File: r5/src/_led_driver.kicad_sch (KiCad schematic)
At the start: 7 parts, among them J16 FH12A-20S-0.5SH, Q22 NX3008NBKW, U9 PCF8574PW

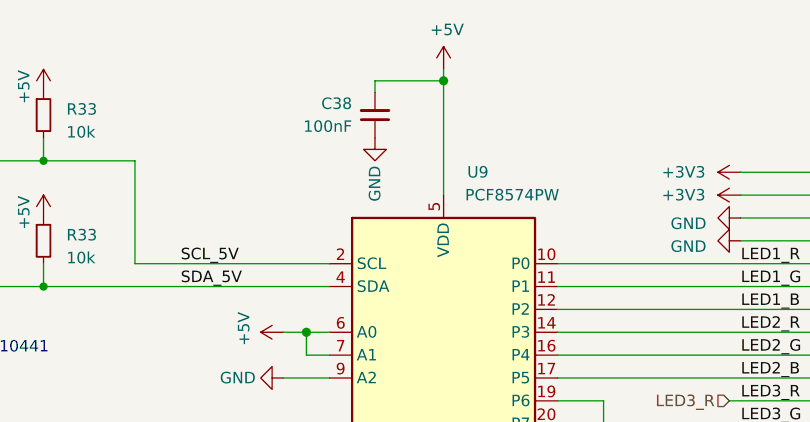
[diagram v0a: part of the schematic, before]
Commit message: Updates to +/-15V supply. Additional output capacitance. Change to smaller inductor packages. Add 0R links to permit isolation of output. Mods to compensation network. Set feedback resistors to datasheet values.
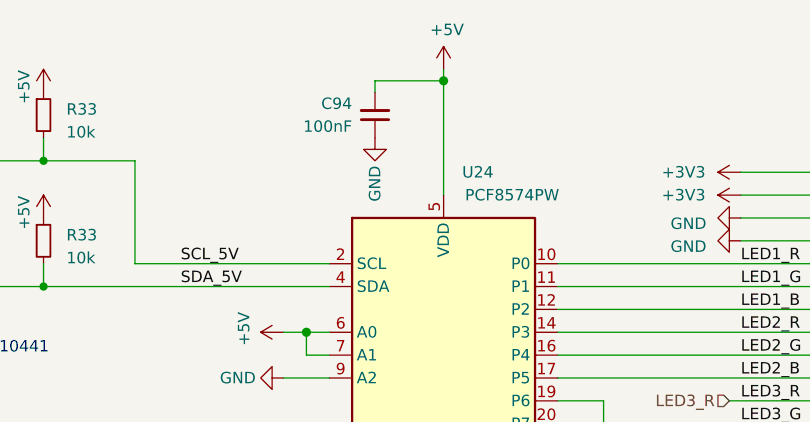
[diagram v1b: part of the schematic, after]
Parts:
- renumbered C38 to C94, U9 to U24
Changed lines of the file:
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@@
   (symbol (lib_id "Interface_Expansion:PCF8574TS") (at 142.24 69.85 0) (unit 1)
     (in_bom yes) (on_board yes) (dnp no)
-    (property "Reference" "U9" (at 146.05 49.53 0)
+    (property "Reference" "U24" (at 146.05 49.53 0)
       (effects (font (size 1.27 1.27)))
     )
@@
       (project "bugg-main-r5"
         (path "/e3eb514f-6ce4-4abe-ba20-f82f0015628f/676be2e4-179b-4538-a96d-4073cd6b4d31"
-          (reference "U9") (unit 1)
+          (reference "U24") (unit 1)
         )
       )
@@
         )
         (path "/e3eb514f-6ce4-4abe-ba20-f82f0015628f/676be2e4-179b-4538-a96d-4073cd6b4d31"
-          (reference "#PWR06") (unit 1)
+          (reference "#PWR0188") (unit 1)
         )
       )
@@
         )
         (path "/e3eb514f-6ce4-4abe-ba20-f82f0015628f/676be2e4-179b-4538-a96d-4073cd6b4d31"
-          (reference "#PWR02") (unit 1)
+          (reference "#PWR0193") (unit 1)
         )
       )
@@
   (symbol (lib_id "power:GND") (at 175.26 57.15 270) (unit 1)
     (in_bom yes) (on_board yes) (dnp no)
-    (property "Reference" "#PWR0125" (at 168.91 57.15 0)
+    (property "Reference" "#PWR0198" (at 168.91 57.15 0)
       (effects (font (size 1.27 1.27)) hide)
     )
@@
       (project "bugg-main-r5"
         (path "/e3eb514f-6ce4-4abe-ba20-f82f0015628f/676be2e4-179b-4538-a96d-4073cd6b4d31"
-          (reference "#PWR0125") (unit 1)
+          (reference "#PWR0198") (unit 1)
         )
       )
@@
   (symbol (lib_id "power:+3V3") (at 175.26 49.53 90) (unit 1)
     (in_bom yes) (on_board yes) (dnp no)
-    (property "Reference" "#PWR0127" (at 179.07 49.53 0)
+    (property "Reference" "#PWR0195" (at 179.07 49.53 0)
       (effects (font (size 1.27 1.27)) hide)
     )
@@
       (project "bugg-main-r5"
         (path "/e3eb514f-6ce4-4abe-ba20-f82f0015628f/676be2e4-179b-4538-a96d-4073cd6b4d31"
-          (reference "#PWR0127") (unit 1)
+          (reference "#PWR0195") (unit 1)
         )
       )
@@
         )
         (path "/e3eb514f-6ce4-4abe-ba20-f82f0015628f/676be2e4-179b-4538-a96d-4073cd6b4d31"
-          (reference "R79") (unit 1)
+          (reference "R66") (unit 1)
         )
       )
@@
   (symbol (lib_id "power:GND") (at 134.62 45.72 0) (unit 1)
     (in_bom yes) (on_board yes) (dnp no)
-    (property "Reference" "#PWR0120" (at 134.62 52.07 0)
+    (property "Reference" "#PWR0192" (at 134.62 52.07 0)
       (effects (font (size 1.27 1.27)) hide)
     )
@@
       (project "bugg-main-r5"
         (path "/e3eb514f-6ce4-4abe-ba20-f82f0015628f/676be2e4-179b-4538-a96d-4073cd6b4d31"
-          (reference "#PWR0120") (unit 1)
+          (reference "#PWR0192") (unit 1)
         )
       )
@@
         )
         (path "/e3eb514f-6ce4-4abe-ba20-f82f0015628f/676be2e4-179b-4538-a96d-4073cd6b4d31"
-          (reference "#PWR03") (unit 1)
+          (reference "#PWR0190") (unit 1)
         )
       )
@@
         )
         (path "/e3eb514f-6ce4-4abe-ba20-f82f0015628f/676be2e4-179b-4538-a96d-4073cd6b4d31"
-          (reference "Q28") (unit 1)
+          (reference "Q13") (unit 1)
         )
       )
@@
         )
         (path "/e3eb514f-6ce4-4abe-ba20-f82f0015628f/676be2e4-179b-4538-a96d-4073cd6b4d31"
-          (reference "R78") (unit 1)
+          (reference "R65") (unit 1)
         )
       )
@@
   (symbol (lib_id "power:+5V") (at 175.26 97.79 90) (unit 1)
     (in_bom yes) (on_board yes) (dnp no)
-    (property "Reference" "#PWR0124" (at 179.07 97.79 0)
+    (property "Reference" "#PWR0199" (at 179.07 97.79 0)
       (effects (font (size 1.27 1.27)) hide)
     )
@@
       (project "bugg-main-r5"
         (path "/e3eb514f-6ce4-4abe-ba20-f82f0015628f/676be2e4-179b-4538-a96d-4073cd6b4d31"
-          (reference "#PWR0124") (unit 1)
+          (reference "#PWR0199") (unit 1)
         )
       )
@@
         )
         (path "/e3eb514f-6ce4-4abe-ba20-f82f0015628f/676be2e4-179b-4538-a96d-4073cd6b4d31"
-          (reference "#PWR05") (unit 1)
+          (reference "#PWR0186") (unit 1)
         )
       )
@@
   (symbol (lib_id "Device:C_Small") (at 134.62 43.18 0) (mirror x) (unit 1)
     (in_bom yes) (on_board yes) (dnp no)
-    (property "Reference" "C38" (at 132.08 41.91 0)
+    (property "Reference" "C94" (at 132.08 41.91 0)
       (effects (font (size 1.27 1.27)) (justify right))
     )
@@
       (project "bugg-main-r5"
         (path "/e3eb514f-6ce4-4abe-ba20-f82f0015628f/676be2e4-179b-4538-a96d-4073cd6b4d31"
-          (reference "C38") (unit 1)
+          (reference "C94") (unit 1)
         )
       )
@@
   (symbol (lib_id "power:GND") (at 142.24 88.9 0) (unit 1)
     (in_bom yes) (on_board yes) (dnp no)
-    (property "Reference" "#PWR0117" (at 142.24 95.25 0)
+    (property "Reference" "#PWR0194" (at 142.24 95.25 0)
       (effects (font (size 1.27 1.27)) hide)
     )
@@
       (project "bugg-main-r5"
         (path "/e3eb514f-6ce4-4abe-ba20-f82f0015628f/676be2e4-179b-4538-a96d-4073cd6b4d31"
-          (reference "#PWR0117") (unit 1)
+          (reference "#PWR0194") (unit 1)
         )
       )
@@
         )
         (path "/e3eb514f-6ce4-4abe-ba20-f82f0015628f/676be2e4-179b-4538-a96d-4073cd6b4d31"
-          (reference "#PWR07") (unit 1)
+          (reference "#PWR0189") (unit 1)
         )
       )
@@
   (symbol (lib_id "power:+3V3") (at 175.26 52.07 90) (unit 1)
     (in_bom yes) (on_board yes) (dnp no)
-    (property "Reference" "#PWR0126" (at 179.07 52.07 0)
+    (property "Reference" "#PWR0196" (at 179.07 52.07 0)
       (effects (font (size 1.27 1.27)) hide)
     )
@@
       (project "bugg-main-r5"
         (path "/e3eb514f-6ce4-4abe-ba20-f82f0015628f/676be2e4-179b-4538-a96d-4073cd6b4d31"
-          (reference "#PWR0126") (unit 1)
+          (reference "#PWR0196") (unit 1)
         )
       )
@@
   (symbol (lib_id "power:GND") (at 124.46 72.39 270) (unit 1)
     (in_bom yes) (on_board yes) (dnp no)
-    (property "Reference" "#PWR0112" (at 118.11 72.39 0)
+    (property "Reference" "#PWR0191" (at 118.11 72.39 0)
       (effects (font (size 1.27 1.27)) hide)
     )
@@
       (project "bugg-main-r5"
         (path "/e3eb514f-6ce4-4abe-ba20-f82f0015628f/676be2e4-179b-4538-a96d-4073cd6b4d31"
-          (reference "#PWR0112") (unit 1)
+          (reference "#PWR0191") (unit 1)
         )
       )
@@
         )
         (path "/e3eb514f-6ce4-4abe-ba20-f82f0015628f/676be2e4-179b-4538-a96d-4073cd6b4d31"
-          (reference "#PWR04") (unit 1)
+          (reference "#PWR0187") (unit 1)
         )
       )
@@
   (symbol (lib_id "power:GND") (at 175.26 54.61 270) (unit 1)
     (in_bom yes) (on_board yes) (dnp no)
-    (property "Reference" "#PWR0128" (at 168.91 54.61 0)
+    (property "Reference" "#PWR0197" (at 168.91 54.61 0)
       (effects (font (size 1.27 1.27)) hide)
     )
@@
       (project "bugg-main-r5"
         (path "/e3eb514f-6ce4-4abe-ba20-f82f0015628f/676be2e4-179b-4538-a96d-4073cd6b4d31"
-          (reference "#PWR0128") (unit 1)
+          (reference "#PWR0197") (unit 1)
         )
       )
@@
   (symbol (lib_id "power:GND") (at 189.23 102.87 0) (unit 1)
     (in_bom yes) (on_board yes) (dnp no)
-    (property "Reference" "#PWR0122" (at 189.23 109.22 0)
+    (property "Reference" "#PWR0200" (at 189.23 109.22 0)
       (effects (font (size 1.27 1.27)) hide)
     )
@@
       (project "bugg-main-r5"
         (path "/e3eb514f-6ce4-4abe-ba20-f82f0015628f/676be2e4-179b-4538-a96d-4073cd6b4d31"
-          (reference "#PWR0122") (unit 1)
+          (reference "#PWR0200") (unit 1)
         )
       )
@@
         )
         (path "/e3eb514f-6ce4-4abe-ba20-f82f0015628f/676be2e4-179b-4538-a96d-4073cd6b4d31"
-          (reference "Q27") (unit 1)
-        )
-      )
+          (reference "Q12") (unit 1)
+        )
+      )

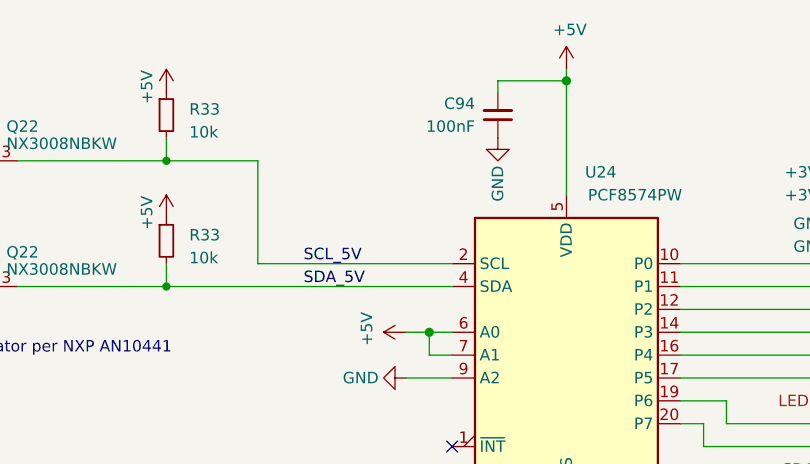
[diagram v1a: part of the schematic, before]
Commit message: Fix broken component annotation by importing back from PCB and fixing duplicates.
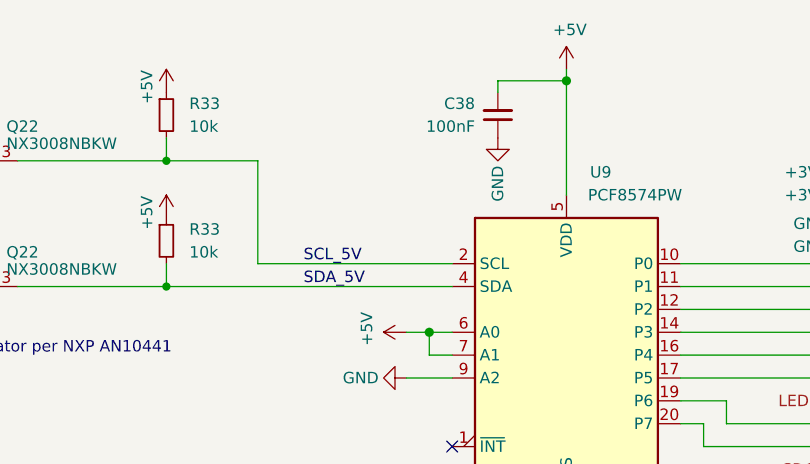
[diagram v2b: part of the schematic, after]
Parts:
- renumbered C94 to C38, U24 to U9
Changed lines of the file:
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@@
   (symbol (lib_id "Interface_Expansion:PCF8574TS") (at 142.24 69.85 0) (unit 1)
     (in_bom yes) (on_board yes) (dnp no)
-    (property "Reference" "U24" (at 146.05 49.53 0)
+    (property "Reference" "U9" (at 146.05 49.53 0)
       (effects (font (size 1.27 1.27)))
     )
@@
       (project "bugg-main-r5"
         (path "/e3eb514f-6ce4-4abe-ba20-f82f0015628f/676be2e4-179b-4538-a96d-4073cd6b4d31"
-          (reference "U24") (unit 1)
+          (reference "U9") (unit 1)
         )
       )
@@
   (symbol (lib_id "Device:R_Small") (at 97.79 57.15 0) (unit 1)
     (in_bom yes) (on_board yes) (dnp no) (fields_autoplaced)
-    (property "Reference" "R33" (at 100.33 56.515 0)
-      (effects (font (size 1.27 1.27)) (justify left))
-    )
-    (property "Value" "10k" (at 100.33 59.055 0)
+    (property "Reference" "R33" (at 100.33 55.88 0)
+      (effects (font (size 1.27 1.27)) (justify left))
+    )
+    (property "Value" "10k" (at 100.33 58.42 0)
       (effects (font (size 1.27 1.27)) (justify left))
     )
@@
         )
         (path "/e3eb514f-6ce4-4abe-ba20-f82f0015628f/676be2e4-179b-4538-a96d-4073cd6b4d31"
-          (reference "R66") (unit 1)
+          (reference "R114") (unit 1)
         )
       )
@@
         )
         (path "/e3eb514f-6ce4-4abe-ba20-f82f0015628f/676be2e4-179b-4538-a96d-4073cd6b4d31"
-          (reference "Q13") (unit 1)
+          (reference "Q28") (unit 1)
         )
       )
@@
   (symbol (lib_id "Device:R_Small") (at 97.79 43.18 0) (unit 1)
     (in_bom yes) (on_board yes) (dnp no) (fields_autoplaced)
-    (property "Reference" "R33" (at 100.33 42.545 0)
-      (effects (font (size 1.27 1.27)) (justify left))
-    )
-    (property "Value" "10k" (at 100.33 45.085 0)
+    (property "Reference" "R33" (at 100.33 41.91 0)
+      (effects (font (size 1.27 1.27)) (justify left))
+    )
+    (property "Value" "10k" (at 100.33 44.45 0)
       (effects (font (size 1.27 1.27)) (justify left))
     )
@@
         )
         (path "/e3eb514f-6ce4-4abe-ba20-f82f0015628f/676be2e4-179b-4538-a96d-4073cd6b4d31"
-          (reference "R65") (unit 1)
+          (reference "R113") (unit 1)
         )
       )
@@
   (symbol (lib_id "Device:C_Small") (at 134.62 43.18 0) (mirror x) (unit 1)
     (in_bom yes) (on_board yes) (dnp no)
-    (property "Reference" "C94" (at 132.08 41.91 0)
+    (property "Reference" "C38" (at 132.08 41.91 0)
       (effects (font (size 1.27 1.27)) (justify right))
     )
@@
       (project "bugg-main-r5"
         (path "/e3eb514f-6ce4-4abe-ba20-f82f0015628f/676be2e4-179b-4538-a96d-4073cd6b4d31"
-          (reference "C94") (unit 1)
+          (reference "C38") (unit 1)
         )
       )
@@
         )
         (path "/e3eb514f-6ce4-4abe-ba20-f82f0015628f/676be2e4-179b-4538-a96d-4073cd6b4d31"
-          (reference "Q12") (unit 1)
-        )
-      )
+          (reference "Q27") (unit 1)
+        )
+      )

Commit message: Update layout to standardise on 0402 passives everywhere possible. This reduces the number of BoM lines. DRC passed. Add DRC exclusions for unavoidable violations
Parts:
- C38: footprint Capacitor_SMD:C_0603_1608Metric -> Capacitor_SMD:C_0402_1005Metric
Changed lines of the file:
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@@
       (effects (font (size 1.27 1.27)) (justify right))
     )
-    (property "Footprint" "Capacitor_SMD:C_0603_1608Metric" (at 134.62 43.18 0)
+    (property "Footprint" "Capacitor_SMD:C_0402_1005Metric" (at 134.62 43.18 0)
       (effects (font (size 1.27 1.27)) hide)
     )

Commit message: Change 0805 47uF to 1206 to save a BOM line. Update layout, DRC pass.
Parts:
- C38: MPN (none) -> GRM155R71H104KE14D; Manufacturer (none) -> Murata; Mouser (none) -> 81-GRM155R71H104KE4D; Voltage (none) -> 50V
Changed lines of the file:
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@@
+      (effects (font (size 1.27 1.27)) hide)
+    )
+    (property "Digikey" "" (at 142.24 69.85 0)
+      (effects (font (size 1.27 1.27)) hide)
+    )
+    (property "MPN" "" (at 142.24 69.85 0)
+      (effects (font (size 1.27 1.27)) hide)
+    )
+    (property "Mouser" "" (at 142.24 69.85 0)
+      (effects (font (size 1.27 1.27)) hide)
+    )
+    (property "Field-1" "" (at 142.24 69.85 0)
       (effects (font (size 1.27 1.27)) hide)
     )
@@
       (effects (font (size 1.27 1.27)) hide)
     )
+    (property "Digikey" "" (at 97.79 57.15 0)
+      (effects (font (size 1.27 1.27)) hide)
+    )
+    (property "MPN" "" (at 97.79 57.15 0)
+      (effects (font (size 1.27 1.27)) hide)
+    )
+    (property "Mouser" "" (at 97.79 57.15 0)
+      (effects (font (size 1.27 1.27)) hide)
+    )
+    (property "Field-1" "" (at 97.79 57.15 0)
+      (effects (font (size 1.27 1.27)) hide)
+    )
     (pin "1")
     (pin "2")
@@
     )
     (property "Quantity" "" (at 76.2 59.69 0)
+      (effects (font (size 1.27 1.27)) hide)
+    )
+    (property "Digikey" "" (at 76.2 59.69 0)
+      (effects (font (size 1.27 1.27)) hide)
+    )
+    (property "MPN" "" (at 76.2 59.69 0)
+      (effects (font (size 1.27 1.27)) hide)
+    )
+    (property "Mouser" "" (at 76.2 59.69 0)
+      (effects (font (size 1.27 1.27)) hide)
+    )
+    (property "Field-1" "" (at 76.2 59.69 0)
       (effects (font (size 1.27 1.27)) hide)
     )
@@
       (effects (font (size 1.27 1.27)) hide)
     )
+    (property "Digikey" "" (at 97.79 43.18 0)
+      (effects (font (size 1.27 1.27)) hide)
+    )
+    (property "MPN" "" (at 97.79 43.18 0)
+      (effects (font (size 1.27 1.27)) hide)
+    )
+    (property "Mouser" "" (at 97.79 43.18 0)
+      (effects (font (size 1.27 1.27)) hide)
+    )
+    (property "Field-1" "" (at 97.79 43.18 0)
+      (effects (font (size 1.27 1.27)) hide)
+    )
     (pin "1")
     (pin "2")
@@
       (effects (font (size 1.27 1.27)) hide)
     )
+    (property "Digikey" "" (at 134.62 43.18 0)
+      (effects (font (size 1.27 1.27)) hide)
+    )
+    (property "MPN" "GRM155R71H104KE14D " (at 134.62 43.18 0)
+      (effects (font (size 1.27 1.27)) hide)
+    )
+    (property "Mouser" "81-GRM155R71H104KE4D " (at 134.62 43.18 0)
+      (effects (font (size 1.27 1.27)) hide)
+    )
+    (property "Field-1" "" (at 134.62 43.18 0)
+      (effects (font (size 1.27 1.27)) hide)
+    )
+    (property "Manufacturer" "Murata" (at 134.62 43.18 0)
+      (effects (font (size 1.27 1.27)) hide)
+    )
+    (property "Voltage" "50V" (at 134.62 43.18 0)
+      (effects (font (size 1.27 1.27)) hide)
+    )
     (pin "1")
     (pin "2")
@@
       (effects (font (size 1.27 1.27)) hide)
     )
+    (property "Digikey" "" (at 76.2 45.72 0)
+      (effects (font (size 1.27 1.27)) hide)
+    )
+    (property "MPN" "" (at 76.2 45.72 0)
+      (effects (font (size 1.27 1.27)) hide)
+    )
+    (property "Mouser" "" (at 76.2 45.72 0)
+      (effects (font (size 1.27 1.27)) hide)
+    )
+    (property "Field-1" "" (at 76.2 45.72 0)
+      (effects (font (size 1.27 1.27)) hide)
+    )
     (pin "1")
     (pin "2")
@@
       (effects (font (size 1.27 1.27)) hide)
     )
+    (property "Digikey" "" (at 189.23 72.39 0)
+      (effects (font (size 1.27 1.27)) hide)
+    )
+    (property "MPN" "" (at 189.23 72.39 0)
+      (effects (font (size 1.27 1.27)) hide)
+    )
+    (property "Mouser" "" (at 189.23 72.39 0)
+      (effects (font (size 1.27 1.27)) hide)
+    )
+    (property "Field-1" "" (at 189.23 72.39 0)
+      (effects (font (size 1.27 1.27)) hide)
+    )
